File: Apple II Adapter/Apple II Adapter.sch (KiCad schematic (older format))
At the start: 23 parts, among them J1 IDC_PORT1, J2 IDC_PORT2, M1 Mounting, U1 74HCT04, U2 CD4066

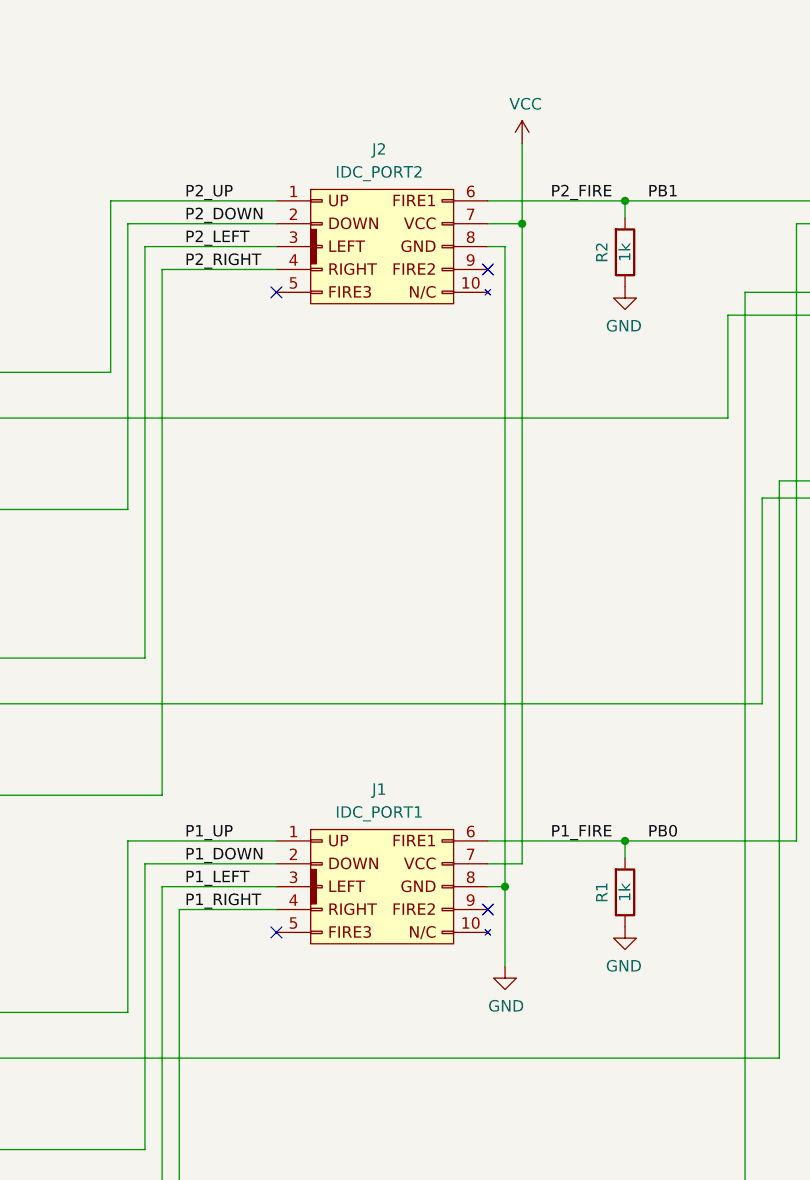
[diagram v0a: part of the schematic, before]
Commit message: Fixed revision A bugs (label and joystick common)
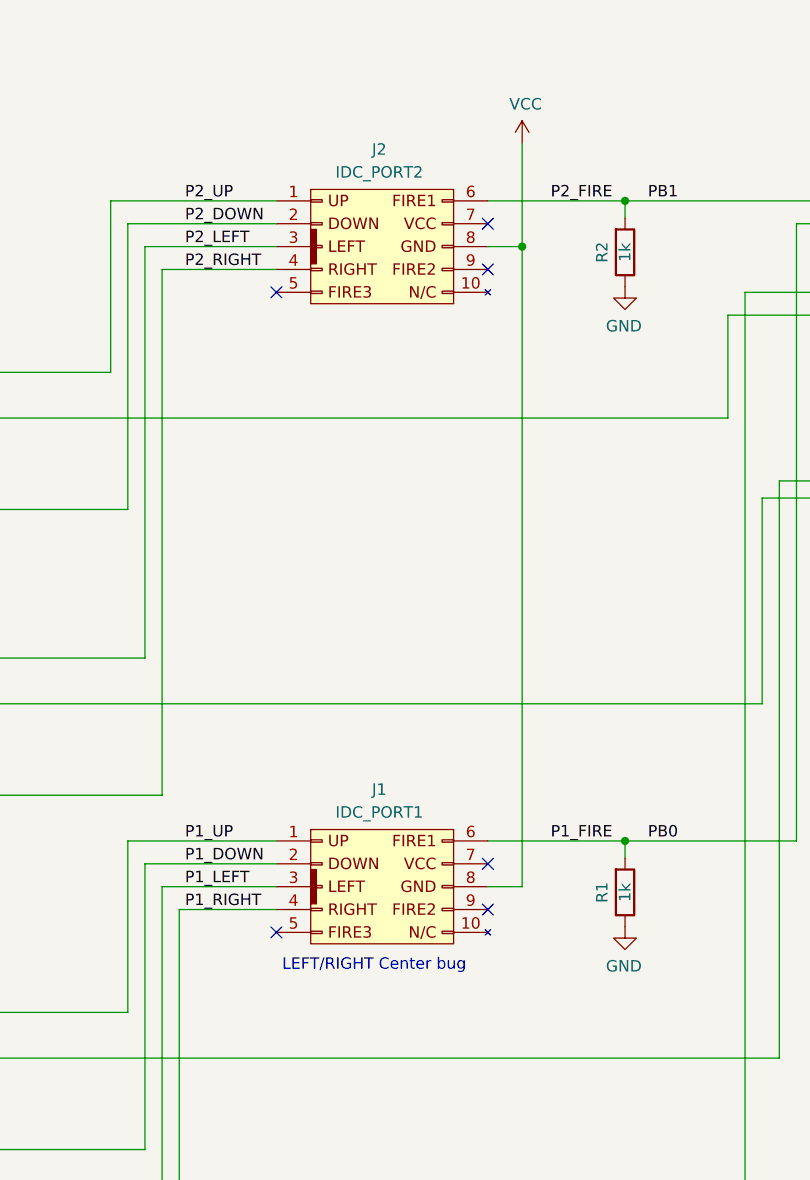
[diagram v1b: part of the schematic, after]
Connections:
- net GND: no longer J1.8 (Pin_8), J2.8 (Pin_8)
- net VCC: now also J1.8 (Pin_8), J2.8 (Pin_8); no longer J1.7 (Pin_7), J2.7 (Pin_7)
- no-connect marks 12 -> 14
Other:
- note added: "LEFT/RIGHT Center bug"
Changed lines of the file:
@@
 Title "Joystick adapter"
 Date ""
-Rev "A"
+Rev "B"
 Comp ""
 Comment1 ""
@@
 NoConn ~ 4850 4500
 NoConn ~ 4850 1700
-Wire Wire Line
-	5850 1500 5775 1500
-$Comp
-L power:GND #PWR03
-U 1 1 5FF9E932
-P 5850 4650
-F 0 "#PWR03" H 5850 4400 50  0001 C CNN
-F 1 "GND" H 5855 4477 50  0000 C CNN
-F 2 "" H 5850 4650 50  0001 C CNN
-F 3 "" H 5850 4650 50  0001 C CNN
-	1    5850 4650
-	1    0    0    -1
-$EndComp
 $Comp
 L apple2_joystick:Game_IO A1
@@
 Wire Wire Line
 	1450 5050 1450 5375
-Text Label 8575 1700 0    50   ~ 0
-GC0
 Text Label 2850 6300 2    50   ~ 0
 GC0
-Text Label 10050 1800 2    50   ~ 0
-GC1
 Text Label 2850 5050 2    50   ~ 0
 GC1
@@
 	1    0    0    -1
 $EndComp
-Wire Wire Line
-	5775 4300 5850 4300
-Connection ~ 5850 4300
-Wire Wire Line
-	5850 4300 5850 4650
 NoConn ~ 5775 4400
 Wire Wire Line
@@
 Wire Wire Line
 	5775 1300 6375 1300
-Wire Wire Line
-	5775 4200 5925 4200
-Wire Wire Line
-	5775 1400 5925 1400
-Wire Wire Line
-	5925 1400 5925 1050
 $Comp
 L power:VCC #PWR0109
@@
 	650  4675 650  5450
 Wire Wire Line
-	5850 1500 5850 4300
-Wire Wire Line
-	5925 1400 5925 4200
-Connection ~ 5925 1400
-Wire Wire Line
 	6825 2250 6825 1800
 Wire Wire Line
@@
 Wire Wire Line
 	2650 6300 6900 6300
+Wire Wire Line
+	5925 1050 5925 1500
+NoConn ~ 5775 1400
+Wire Wire Line
+	5775 1500 5925 1500
+Connection ~ 5925 1500
+Wire Wire Line
+	5775 4300 5925 4300
+Wire Wire Line
+	5925 1500 5925 4300
+NoConn ~ 5775 4200
+Text Notes 4875 4675 0    50   ~ 0
+LEFT/RIGHT Center bug
+Text Label 10050 1800 2    50   ~ 0
+GC1
+Text Label 8575 1700 0    50   ~ 0
+GC0
 $EndSCHEMATC

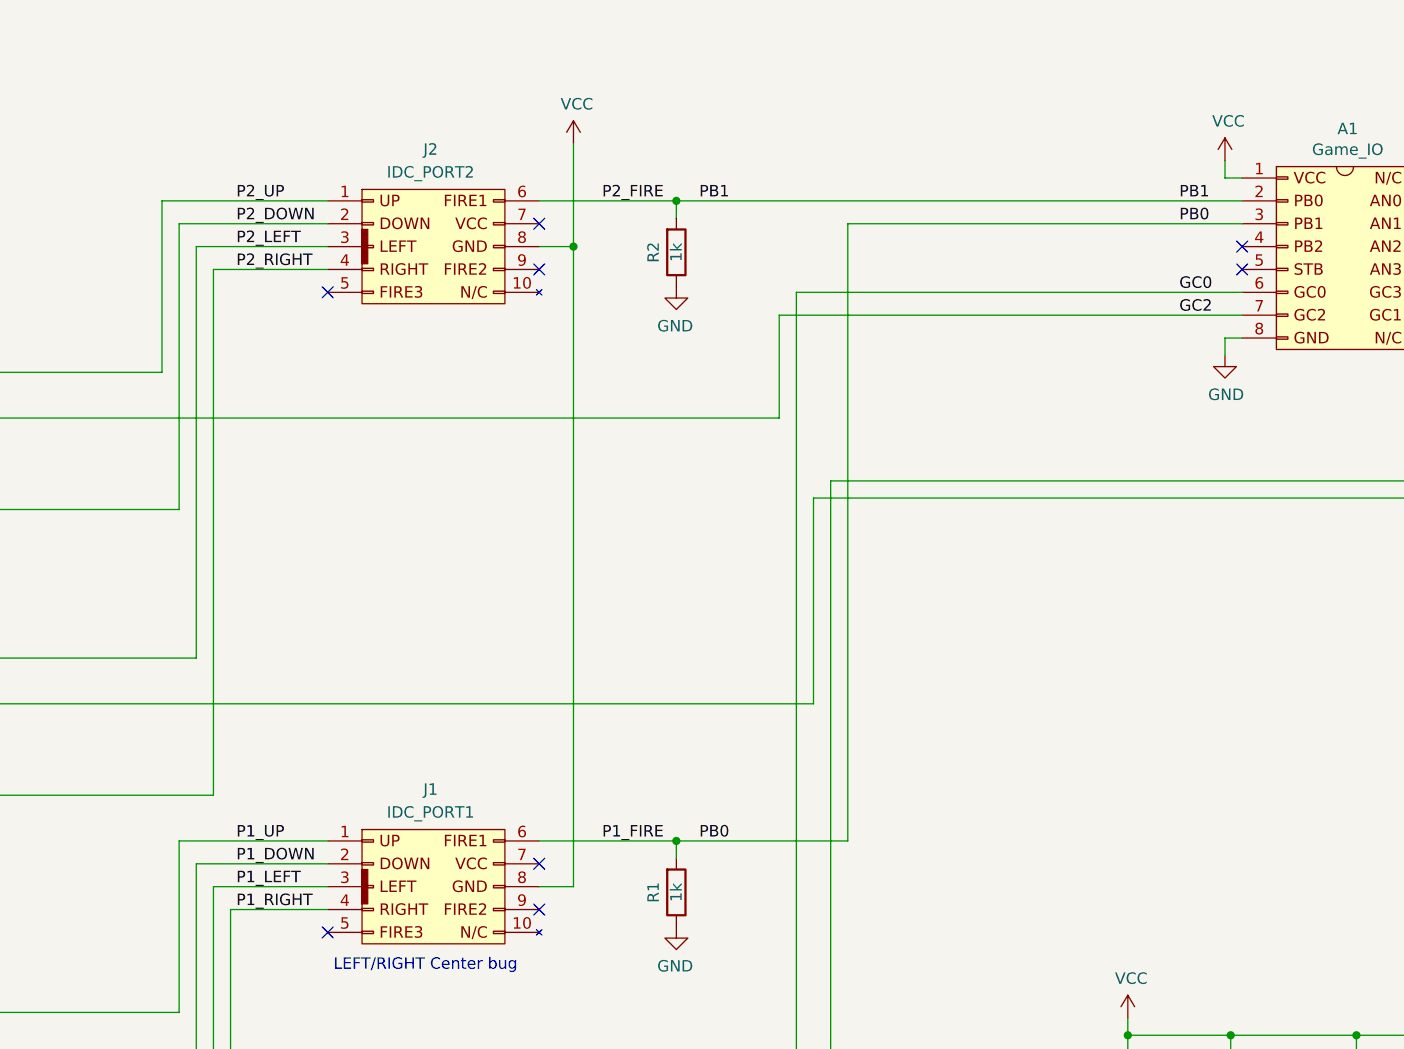
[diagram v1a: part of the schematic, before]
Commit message: Swapped fire buttons
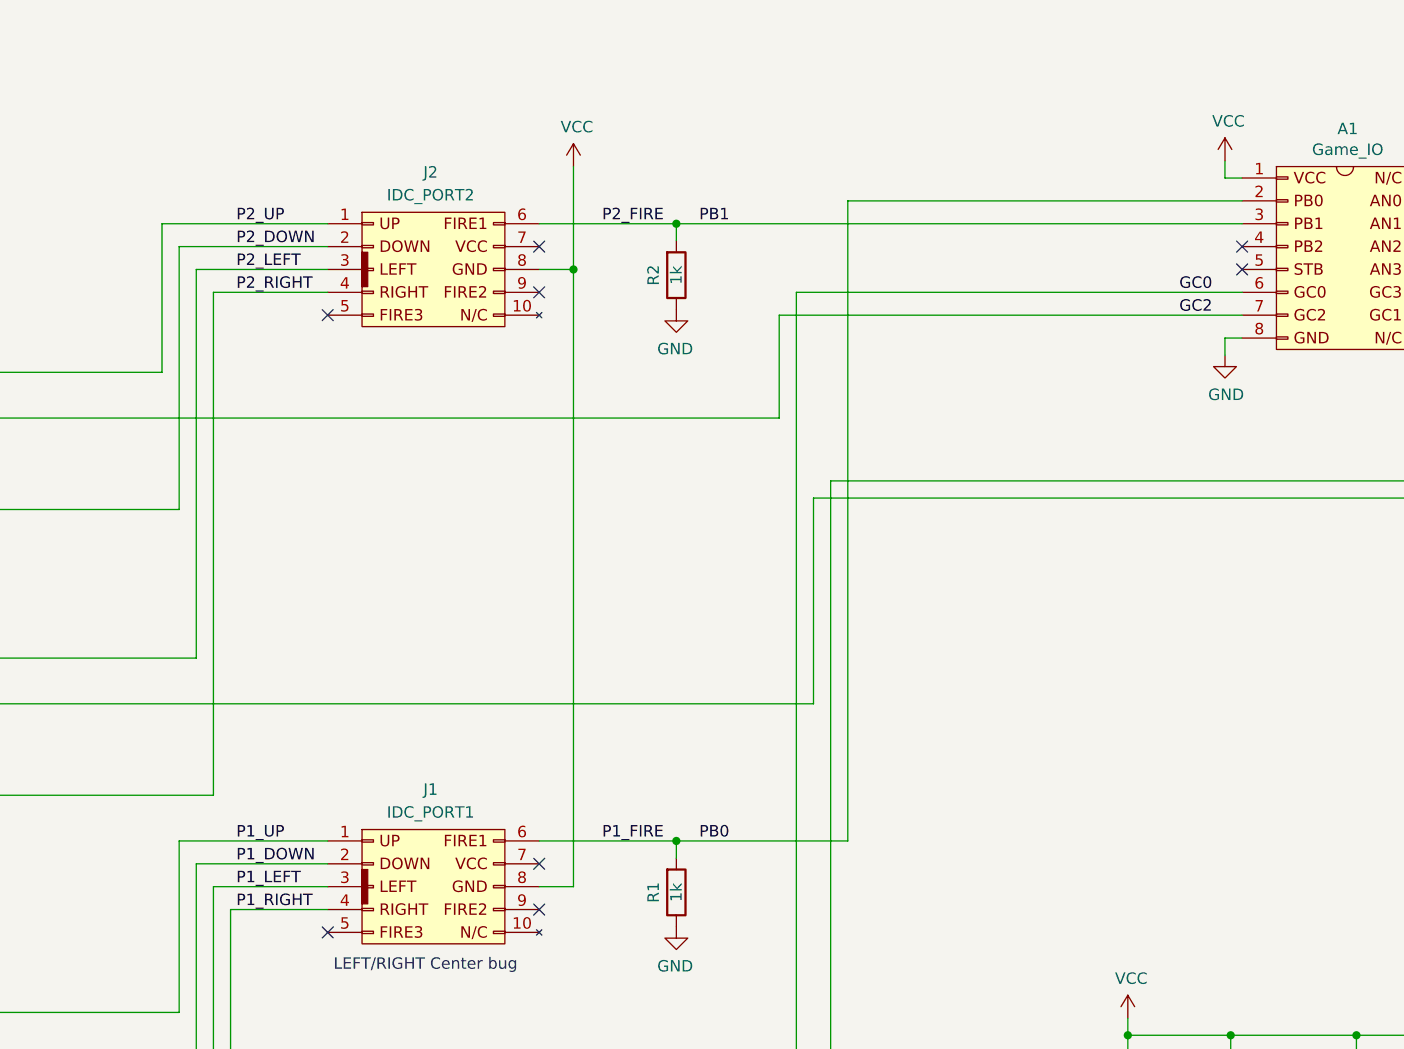
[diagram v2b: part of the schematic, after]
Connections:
- net P1_FIRE: now also A1.2 (PB0); no longer A1.3 (PB1)
- net P2_FIRE: now also A1.3 (PB1); no longer A1.2 (PB0)
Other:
- moved on the sheet: J2, R2
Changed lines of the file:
@@
 L c64_joykey:C64_IDC2_OUT J2
 U 1 1 5FF9E0A1
-P 5300 1500
-F 0 "J2" H 5300 1925 50  0000 C CNN
-F 1 "IDC_PORT2" H 5300 1825 50  0000 C CNN
-F 2 "C64 JoyKEY:IDC_Joystick" H 5325 1175 50  0001 C CNN
-F 3 "" H 5325 1175 50  0001 C CNN
-	1    5300 1500
-	1    0    0    -1
-$EndComp
-NoConn ~ 5775 1600
+P 5300 1600
+F 0 "J2" H 5300 2025 50  0000 C CNN
+F 1 "IDC_PORT2" H 5300 1925 50  0000 C CNN
+F 2 "C64 JoyKEY:IDC_Joystick" H 5325 1275 50  0001 C CNN
+F 3 "" H 5325 1275 50  0001 C CNN
+	1    5300 1600
+	1    0    0    -1
+$EndComp
+NoConn ~ 5775 1700
 NoConn ~ 4850 4500
-NoConn ~ 4850 1700
+NoConn ~ 4850 1800
 $Comp
 L apple2_joystick:Game_IO A1
@@
 Text Label 10050 1700 2    50   ~ 0
 GC3
-Text Label 8575 1400 0    50   ~ 0
-PB0
-Text Label 8575 1300 0    50   ~ 0
-PB1
 $Comp
 L Device:R R14
@@
 Text Label 2850 2250 2    50   ~ 0
 GC2
-Text Label 4450 1300 0    50   ~ 0
+Text Label 4450 1400 0    50   ~ 0
 P2_UP
 Text Label 2850 2050 2    50   ~ 0
@@
 	2200 3225 2200 3300
 Connection ~ 2200 3300
-Text Label 4450 1500 0    50   ~ 0
+Text Label 4450 1600 0    50   ~ 0
 P2_LEFT
 Text Label 2850 3300 2    50   ~ 0
@@
 Text Label 2850 6100 2    50   ~ 0
 P1_LEFT
-Text Label 6475 1300 0    50   ~ 0
+Text Label 6475 1400 0    50   ~ 0
 PB1
 $Comp
 L Device:R R2
 U 1 1 60051E25
-P 6375 1525
-F 0 "R2" V 6275 1525 50  0000 C CNN
-F 1 "1k" V 6375 1525 50  0000 C CNN
-F 2 "Resistor_THT:R_Axial_DIN0207_L6.3mm_D2.5mm_P10.16mm_Horizontal" V 6305 1525 50  0001 C CNN
-F 3 "~" H 6375 1525 50  0001 C CNN
-	1    6375 1525
+P 6375 1625
+F 0 "R2" V 6275 1625 50  0000 C CNN
+F 1 "1k" V 6375 1625 50  0000 C CNN
+F 2 "Resistor_THT:R_Axial_DIN0207_L6.3mm_D2.5mm_P10.16mm_Horizontal" V 6305 1625 50  0001 C CNN
+F 3 "~" H 6375 1625 50  0001 C CNN
+	1    6375 1625
 	1    0    0    1
 $EndComp
 Wire Wire Line
-	6375 1300 6375 1375
+	6375 1400 6375 1475
 $Comp
 L power:GND #PWR0106
 U 1 1 60055CF8
-P 6375 1675
-F 0 "#PWR0106" H 6375 1425 50  0001 C CNN
-F 1 "GND" H 6380 1502 50  0000 C CNN
-F 2 "" H 6375 1675 50  0001 C CNN
-F 3 "" H 6375 1675 50  0001 C CNN
-	1    6375 1675
+P 6375 1775
+F 0 "#PWR0106" H 6375 1525 50  0001 C CNN
+F 1 "GND" H 6380 1602 50  0000 C CNN
+F 2 "" H 6375 1775 50  0001 C CNN
+F 3 "" H 6375 1775 50  0001 C CNN
+	1    6375 1775
 	-1   0    0    -1
 $EndComp
@@
 	-1   0    0    -1
 $EndComp
-Text Label 6050 1300 0    50   ~ 0
+Text Label 6050 1400 0    50   ~ 0
 P2_FIRE
-Connection ~ 6375 1300
 Text Label 6050 4100 0    50   ~ 0
 P1_FIRE
@@
 	5775 4100 6375 4100
 Wire Wire Line
-	5775 1300 6375 1300
+	5775 1400 6375 1400
 $Comp
 L power:VCC #PWR0109
 U 1 1 60097DDF
-P 5925 1050
-F 0 "#PWR0109" H 5925 900 50  0001 C CNN
-F 1 "VCC" H 5940 1223 50  0000 C CNN
-F 2 "" H 5925 1050 50  0001 C CNN
-F 3 "" H 5925 1050 50  0001 C CNN
-	1    5925 1050
+P 5925 1150
+F 0 "#PWR0109" H 5925 1000 50  0001 C CNN
+F 1 "VCC" H 5940 1323 50  0000 C CNN
+F 2 "" H 5925 1150 50  0001 C CNN
+F 3 "" H 5925 1150 50  0001 C CNN
+	1    5925 1150
 	1    0    0    -1
 $EndComp
@@
 Wire Wire Line
 	1825 1875 1750 1875
-Text Label 4450 1400 0    50   ~ 0
+Text Label 4450 1500 0    50   ~ 0
 P2_DOWN
 Text Label 675  1875 0    50   ~ 0
@@
 Wire Wire Line
 	650  3125 1075 3125
-Text Label 4450 1600 0    50   ~ 0
+Text Label 4450 1700 0    50   ~ 0
 P2_RIGHT
 $Comp
@@
 	650  2650 4200 2650
 Wire Wire Line
-	4200 1400 4850 1400
+	4200 1500 4850 1500
 Wire Wire Line
 	2200 3300 4275 3300
 Wire Wire Line
-	4275 1500 4850 1500
+	4275 1600 4850 1600
 Wire Wire Line
 	650  3125 650  3900
 Wire Wire Line
-	4350 1600 4850 1600
+	4350 1700 4850 1700
 Wire Wire Line
 	650  3900 4350 3900
@@
 	2200 1975 2200 2050
 Wire Wire Line
-	4350 1600 4350 3900
-Wire Wire Line
-	4275 1500 4275 3300
-Wire Wire Line
-	4200 1400 4200 2650
-Wire Wire Line
 	2200 2050 4125 2050
 Wire Wire Line
-	4125 2050 4125 1300
-Wire Wire Line
-	4125 1300 4850 1300
+	4125 1400 4850 1400
 Connection ~ 2200 2050
 Wire Wire Line
@@
 NoConn ~ 8850 1600
 Wire Wire Line
-	6375 1300 8850 1300
-Wire Wire Line
 	6825 1800 8850 1800
 Wire Wire Line
@@
 Wire Wire Line
 	7050 2525 10125 2525
-Wire Wire Line
-	7125 1400 8850 1400
-Wire Wire Line
-	7125 1400 7125 4100
 Wire Wire Line
 	6375 4100 7125 4100
@@
 	2650 6300 6900 6300
 Wire Wire Line
-	5925 1050 5925 1500
-NoConn ~ 5775 1400
-Wire Wire Line
-	5775 1500 5925 1500
-Connection ~ 5925 1500
+	5925 1150 5925 1600
+NoConn ~ 5775 1500
+Wire Wire Line
+	5775 1600 5925 1600
 Wire Wire Line
 	5775 4300 5925 4300
-Wire Wire Line
-	5925 1500 5925 4300
 NoConn ~ 5775 4200
 Text Notes 4875 4675 0    50   ~ 0
@@
 Text Label 8575 1700 0    50   ~ 0
 GC0
+Wire Wire Line
+	8850 1300 7125 1300
+Wire Wire Line
+	7125 1300 7125 4100
+Connection ~ 5925 1600
+Wire Wire Line
+	6375 1400 8850 1400
+Connection ~ 6375 1400
+Wire Wire Line
+	4350 1700 4350 3900
+Wire Wire Line
+	4275 1600 4275 3300
+Wire Wire Line
+	4200 1500 4200 2650
+Wire Wire Line
+	4125 1400 4125 2050
+Wire Wire Line
+	5925 1600 5925 4300
 $EndSCHEMATC

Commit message: Removed leftover notes
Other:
- note removed: "LEFT/RIGHT Center bug"
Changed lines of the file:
@@
 	5775 4300 5925 4300
 NoConn ~ 5775 4200
-Text Notes 4875 4675 0    50   ~ 0
-LEFT/RIGHT Center bug
 Text Label 10050 1800 2    50   ~ 0
 GC1
